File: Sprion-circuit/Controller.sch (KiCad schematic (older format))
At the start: 22 parts, among them J2 Conn_01x04_Female, Q3 Q_NMOS_GSD, Q4 Q_NMOS_GSD, SW2 SW_Push, SW3 SW_Push, SW4 SW_Push, U3 STM32F405RGTx

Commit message: add,feat,fix:すまんコミットわすれててぐちゃぐちゃや
配置始めた。
フットプリント割り当てた
回路図pdfで吐いた
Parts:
- added C14: 4.7u, Capacitor_SMD:C_0603_1608Metric, symbol Device:C
- added C3: 0.1u, Capacitor_SMD:C_0603_1608Metric, symbol Device:C
- added J6: Conn_01x04_Female, Connector_JST:JST_SH_SM04B-SRSS-TB_1x04-1MP_P1.00mm_Horizontal, symbol Connector:Conn_01x04_Female
- 2.2k1: renamed from 2.2k; footprint (none) -> Sprion-circuit:Potentiometer_SMD_PVZ3A
- C28, C29, C30, C31, C32, C33, C34, C35: footprint (none) -> Capacitor_SMD:C_0603_1608Metric
- J2: footprint (none) -> Connector_JST:JST_SH_SM04B-SRSS-TB_1x04-1MP_P1.00mm_Horizontal
- LS1: footprint (none) -> Sprion-circuit:PKMCS
- Q3: value Q_NMOS_GSD -> IRFML8244; footprint (none) -> Package_TO_SOT_SMD:SOT-23
- Q4: value Q_NMOS_GSD -> RUE002N02; footprint (none) -> Package_TO_SOT_SMD:SOT-416
- R34, R36, R37: footprint (none) -> Resistor_SMD:R_0603_1608Metric
- R35: value 500 -> 1k; footprint (none) -> Resistor_SMD:R_0603_1608Metric
- SW2, SW3, SW4: footprint (none) -> Sprion-circuit:SMT_4.2X3.2_
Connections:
- net +3V3: now also C14.1, C3.1, J6.1 (Pin_1)
- net +BATT: now also 2.2k1.1; no longer R35.1
- net GND: now also J2.2 (Pin_2), C14.2, C3.2, J6.4 (Pin_4); no longer J2.4 (Pin_4)
- net RESET: now also J2.4 (Pin_4); no longer J2.1 (Pin_1)
- net SWDCLK: now also J2.1 (Pin_1); no longer J2.3 (Pin_3)
- net SWDIO: now also J2.3 (Pin_3); no longer J2.2 (Pin_2)
- net UART_TX: now reaches U3.14 (PA0)
- net UART_TX: now also J6.3 (Pin_3)
- net UART_RX: now reaches U3.15 (PA1)
- net UART_RX: now also J6.2 (Pin_2)
- net at LS1.2, Q3.3 (D): now also R35.2; no longer 2.2k1.2
- new net: 2.2k1.2, LS1.1, R35.1
- no-connect marks 24 -> 22
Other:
- note removed: "TIM5\n"
- moved on the sheet: 2.2k1, C30, C31, C32, C33, C34, D10, J2, LS1, Q3, Q4, R34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

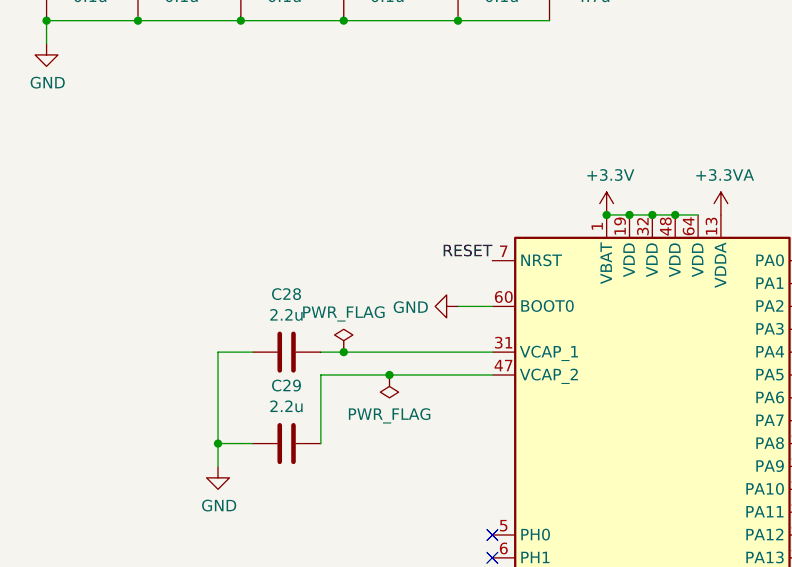
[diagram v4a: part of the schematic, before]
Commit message: fix: eschemaの微修正
ハイサイドスイッチをNch→Pchへ修正
bootをプルダウンに
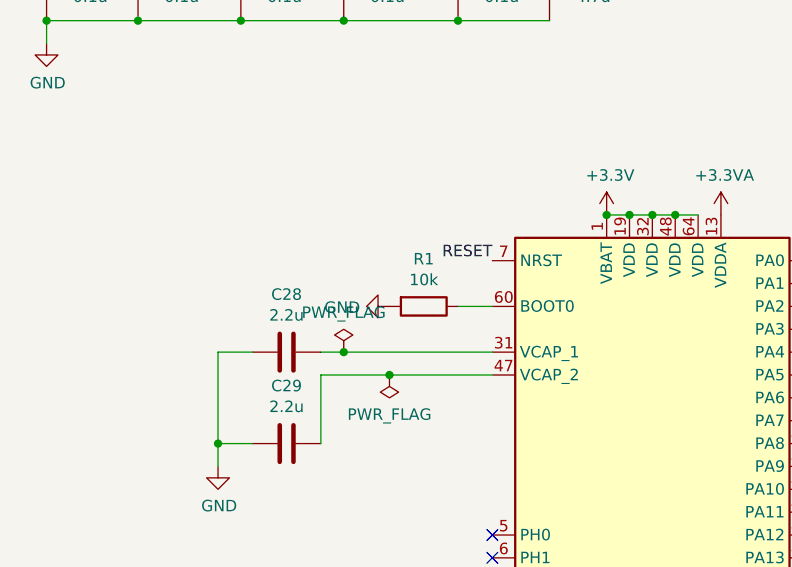
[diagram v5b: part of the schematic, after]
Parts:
- added R1: 10k, Resistor_SMD:R_0603_1608Metric, symbol Device:R
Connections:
- net GND: now also R1.2; no longer U3.60 (BOOT0)
- new net: R1.1, U3.60 (BOOT0)
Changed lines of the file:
@@
 L power:GND #PWR073
 U 1 1 60EE357E
-P 2400 2750
-F 0 "#PWR073" H 2400 2500 50  0001 C CNN
-F 1 "GND" V 2405 2622 50  0000 R CNN
-F 2 "" H 2400 2750 50  0001 C CNN
-F 3 "" H 2400 2750 50  0001 C CNN
-	1    2400 2750
+P 2100 2750
+F 0 "#PWR073" H 2100 2500 50  0001 C CNN
+F 1 "GND" V 2105 2622 50  0000 R CNN
+F 2 "" H 2100 2750 50  0001 C CNN
+F 3 "" H 2100 2750 50  0001 C CNN
+	1    2100 2750
 	0    1    1    0
 $EndComp
@@
 Wire Wire Line
 	6400 1500 6500 1500
+$Comp
+L Device:R R1
+U 1 1 61B55E3E
+P 2250 2750
+F 0 "R1" V 2043 2750 50  0000 C CNN
+F 1 "10k" V 2134 2750 50  0000 C CNN
+F 2 "Resistor_SMD:R_0603_1608Metric" V 2180 2750 50  0001 C CNN
+F 3 "~" H 2250 2750 50  0001 C CNN
+	1    2250 2750
+	0    1    1    0
+$EndComp
 $EndSCHEMATC

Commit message: add fix feat: でけたー（コミットしてなくてごめん）
ベタ塗、配線、再配置等
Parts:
- removed D10: SK6812MINI, LED_SMD:LED_SK6812MINI_PLCC4_3.5x3.5mm_P1.75mm, symbol LED:SK6812MINI
- added D?: SK6812MINI, symbol Sprion-circuit:SK6812MINI
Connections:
- net +5V: now also D?.2 (VDD)
- net GND: now also D?.4 (VSS)
- net at Q4.3 (D), R37.2: now also D?.1 (DIN)
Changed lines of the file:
@@
 $Descr A4 11693 8268
 encoding utf-8
-Sheet 5 6
+Sheet 4 6
 Title ""
 Date ""
@@
 	1350 2950 1350 3350
 Connection ~ 1350 3350
-$Comp
-L LED:SK6812MINI D10
-U 1 1 60EFAFD7
-P 10000 5300
-F 0 "D10" H 10344 5346 50  0000 L CNN
-F 1 "SK6812MINI" H 10344 5255 50  0000 L CNN
-F 2 "LED_SMD:LED_SK6812MINI_PLCC4_3.5x3.5mm_P1.75mm" H 10050 5000 50  0001 L TNN
-F 3 "https://cdn-shop.adafruit.com/product-files/2686/SK6812MINI_REV.01-1-2.pdf" H 10100 4925 50  0001 L TNN
-	1    10000 5300
-	1    0    0    -1
-$EndComp
 Wire Wire Line
 	2300 4650 2550 4650
@@
 	0    1    1    0
 $EndComp
+$Comp
+L Sprion-circuit:SK6812MINI D?
+U 1 1 61C04E87
+P 10000 5300
+F 0 "D?" H 10344 5346 50  0000 L CNN
+F 1 "SK6812MINI" H 10344 5255 50  0000 L CNN
+F 2 "" H 10000 5750 50  0001 C CNN
+F 3 "" H 10000 5750 50  0001 C CNN
+	1    10000 5300
+	1    0    0    -1
+$EndComp
 $EndSCHEMATC
